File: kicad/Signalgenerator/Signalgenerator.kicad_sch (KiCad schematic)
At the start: 18 parts, among them U1 LT1354CS8, U2 LT1354CS8, U3 LT1354CS8, U4 LT1354CS8, U5 LT1354CS8, U6 LT1354CS8, U7 LT1354CS8

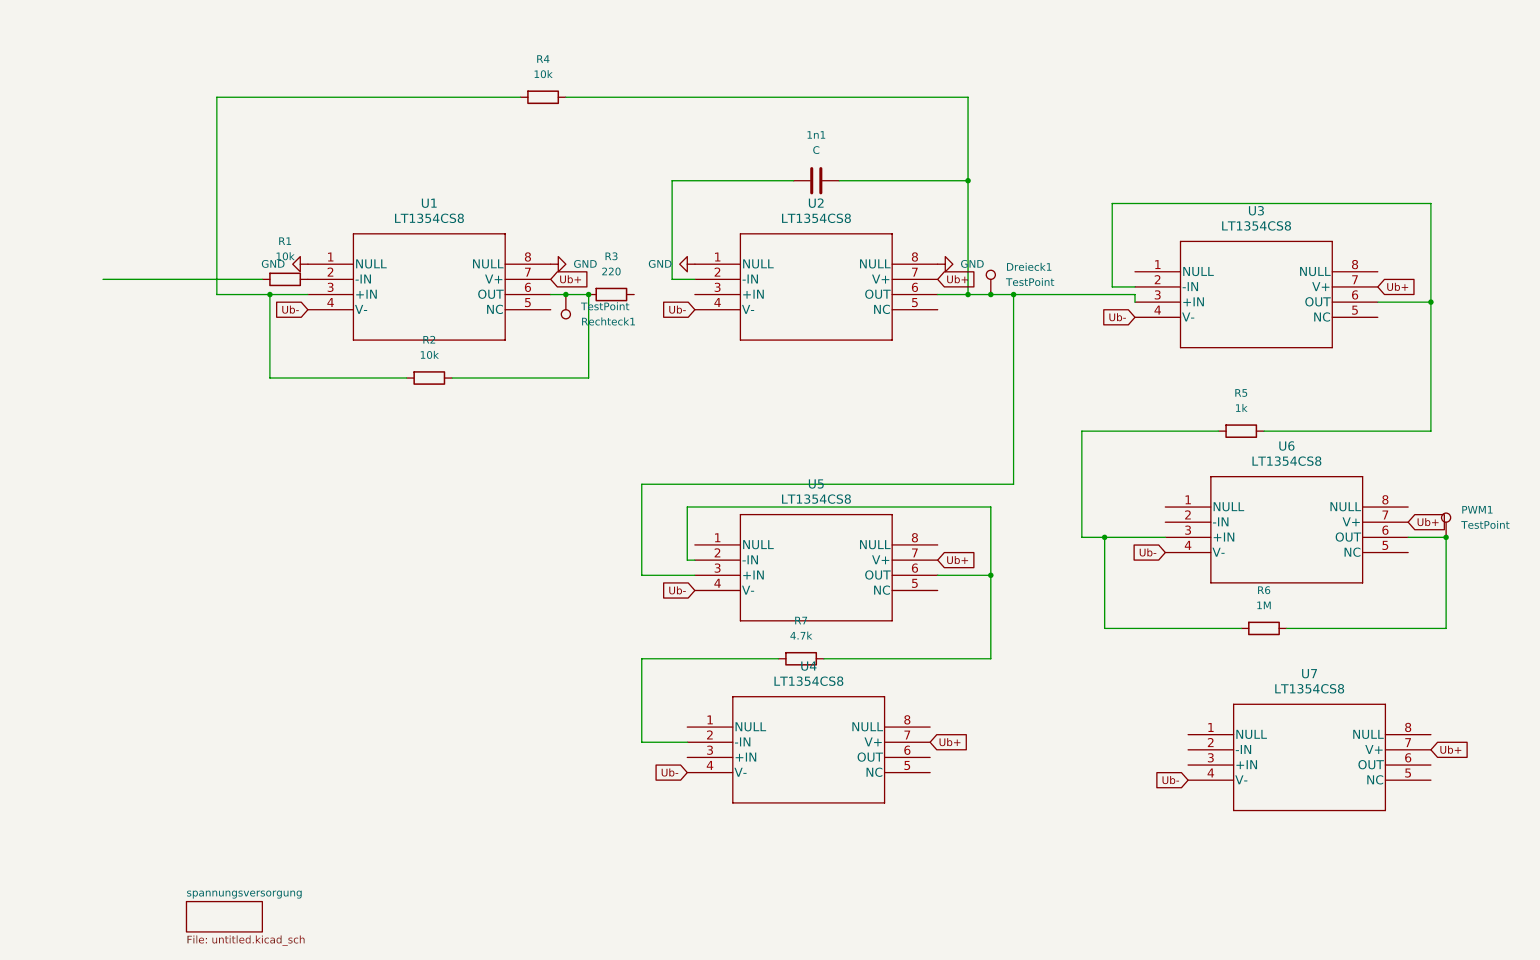
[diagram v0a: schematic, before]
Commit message: Platine layout angefangen. Probleme mit Überkreuzungen.
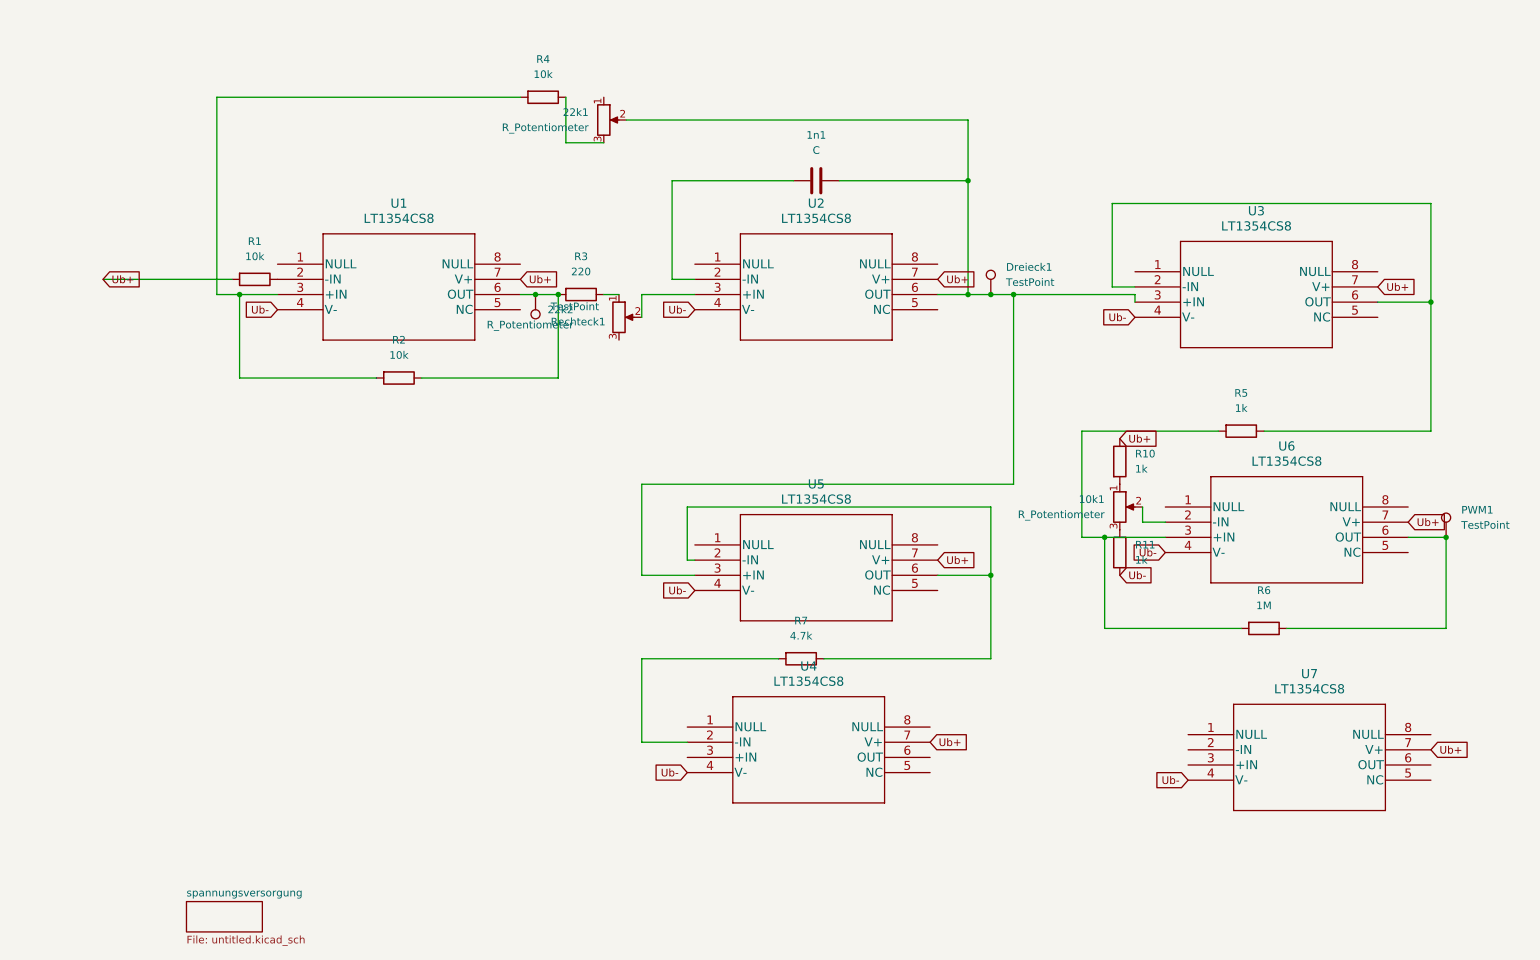
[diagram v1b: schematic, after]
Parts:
- added 10k1, 22k1, 22k2: R_Potentiometer, Potentiometer_THT:Potentiometer_Vishay_T7-YA_Single_Vertical, symbol Device:R_Potentiometer
- added R10, R11: 1k, Resistor_SMD:R_0805_2012Metric_Pad1.20x1.40mm_HandSolder, symbol Device:R
- 1n1: footprint (none) -> Capacitor_SMD:C_0603_1608Metric_Pad1.08x0.95mm_HandSolder
- R1, R2, R3, R4, R5, R6, R7: footprint (none) -> Resistor_SMD:R_0805_2012Metric_Pad1.20x1.40mm_HandSolder
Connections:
- net Ub+: now also R1.2, R10.1
- net Ub-: now also R11.1
- net at 1n1.1, Dreieck1.1, U2.6 (OUT)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: now also 22k1.2; no longer R4.1
- net at R3.1: now also 22k2.1
- net at U2.3 (+IN): now also 22k2.2
- net at U6.2 (-IN): now also 10k1.2
- removed net GND: U1.1 (NULL), U1.8 (NULL), U2.1 (NULL), U2.8 (NULL)
- new net: 22k1.3, R4.1
- new net: 10k1.3, R11.2
- new net: 10k1.1, R10.2
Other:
- moved on the sheet: R1, R2, R3, Rechteck1, U1

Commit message: kleine änderungen
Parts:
- R4: value 10k -> 1k
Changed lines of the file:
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@@
 			)
 		)
-		(property "Value" "10k"
+		(property "Value" "1k"
 			(at 106.68 21.59 90)
 			(effects

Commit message: layout zwischenstand
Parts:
- added C10, C11, C12, C13, C14, C15, C16, C17, C18, C19, C20, C7, C8, C9: 0.1u, Capacitor_SMD:C_0603_1608Metric_Pad1.08x0.95mm_HandSolder, symbol Device:C
- added C22: 1n, Capacitor_SMD:C_0603_1608Metric_Pad1.08x0.95mm_HandSolder, symbol Device:C
- added C23: 100p, Capacitor_SMD:C_0603_1608Metric_Pad1.08x0.95mm_HandSolder, symbol Device:C
- added C6: 10n, Capacitor_SMD:C_0603_1608Metric_Pad1.08x0.95mm_HandSolder, symbol Device:C
- added D1: D, Diode_THT:D_A-405_P2.54mm_Vertical_AnodeUp, symbol Device:D
- added R12: 1k, Resistor_SMD:R_0805_2012Metric_Pad1.20x1.40mm_HandSolder, symbol Device:R
- added R13: 10k, Resistor_SMD:R_0805_2012Metric_Pad1.20x1.40mm_HandSolder, symbol Device:R
- added R14, R15, R16: 0, Resistor_SMD:R_0805_2012Metric_Pad1.20x1.40mm_HandSolder, symbol Device:R
- added RV1, RV2: R_Potentiometer, Potentiometer_THT:Potentiometer_Vishay_T7-YA_Single_Vertical, symbol Device:R_Potentiometer
- added SW1, SW3: OS103011MS8QP1, footprints:OS103011MS8QP1, symbol 2026-05-24_19-47-42:OS103011MS8QP1
- added SW2: SW_DPDT_x2, Button_Switch_THT:SW_Slide_SPDT_Straight_CK_OS102011MS2Q, symbol Switch:SW_DPDT_x2
- C24: renamed from 1n1; value C -> 10n
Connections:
- net Ub+: now also C10.2, C12.2, C14.2, C16.2, C18.2, C20.2, C8.2, R14.1, R14.2, RV2.1
- net Ub-: now also C11.1, C13.1, C15.1, C17.1, C19.1, C7.1, C9.1, R15.1, R15.2, RV2.3
- net at Dreieck1.1, U2.6 (OUT), U5.3 (+IN): now also R16.2, SW1.2, SW3.3; no longer 22k1.2, C24.1, U3.3 (+IN)
- net at C24.2, U2.2 (-IN): now also 22k1.2, C22.1, C23.1
- net at 22k2.1, R3.1: now also D1.2 (A)
- net at 22k2.2: now also SW2.1 (A); no longer U2.3 (+IN)
- net at R5.2, R6.2, U6.3 (+IN): now also SW3.1
- net at U7.2 (-IN): now also R12.2, RV1.3
- net at U7.3 (+IN): now also SW3.2
- net at U7.6 (OUT): now also RV1.2
- net at R7.2, U4.2 (-IN): now also C6.2, R13.2
- net GND: now reaches U4.3 (+IN)
- net GND: now also C10.1, C11.2, C12.1, C13.2, C14.1, C15.2, C16.1, C17.2, C18.1, C19.2, C20.1, C7.2, C8.1, C9.2
- net at U4.6 (OUT): now also C6.1, R13.1, SW3.4
- new net: R12.1, RV2.2
- new net: R16.1, U3.3 (+IN)
- new net: C24.1, SW1.1
- new net: C23.2, SW1.4
- new net: D1.1 (K), SW2.3 (C)
- new net: C22.2, SW1.3
- new net: SW2.2 (B), U2.3 (+IN)
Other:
- moved on the sheet: 22k1, 22k2, R1, R2, R3, R4, R7, Rechteck1, U1, U4, U5

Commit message: aktueller stand
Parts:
- added R17, R18: 0, Resistor_SMD:R_0805_2012Metric_Pad1.20x1.40mm_HandSolder, symbol Device:R
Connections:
- net at Dreieck1.1, R16.2, SW1.2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: now also R17.1; no longer U2.6 (OUT)
- net at 22k1.2, C22.1, C23.1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: now also R18.1; no longer U2.2 (-IN)
- new net: R17.2, U2.6 (OUT)
- new net: R18.2, U2.2 (-IN)
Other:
- moved on the sheet: D1, Dreieck1, SW2A

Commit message: schaltplan angepasst
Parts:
- removed C11, C13, C15, C17, C19, C7, C9: 0.1u, Capacitor_SMD:C_0603_1608Metric_Pad1.08x0.95mm_HandSolder, symbol Device:C
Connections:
- net GND: no longer C10.1, C12.1, C14.1, C16.1, C18.1, C20.1, C8.1
- net Ub-: now also C10.1, C12.1, C14.1, C16.1, C18.1, C20.1, C8.1

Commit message: stand jetzt
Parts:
- removed R16, R17, R18: 0, Resistor_SMD:R_0805_2012Metric_Pad1.20x1.40mm_HandSolder, symbol Device:R
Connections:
- net at U3.3 (+IN): now also Dreieck1.1, SW1.2, SW3.3, U2.6 (OUT), U5.3 (+IN)
- net at 22k1.2, C22.1, C23.1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: now also U2.2 (-IN)
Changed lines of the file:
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@@
 	)
 	(junction
-		(at 185.42 58.42)
+		(at 90.17 58.42)
 		(diameter 0)
 		(color 0 0 0 0)
 	)
 	(junction
-		(at 90.17 58.42)
+		(at 181.61 58.42)
 		(diameter 0)
 		(color 0 0 0 0)
 	)
 	(junction
-		(at 181.61 58.42)
+		(at 185.42 58.42)
 		(diameter 0)
 		(color 0 0 0 0)
@@
 	(wire
 		(pts
-			(xy 172.72 58.42) (xy 173.99 58.42)
+			(xy 172.72 58.42) (xy 181.61 58.42)
 		)
 		(stroke
@@
 	(wire
 		(pts
-			(xy 128.27 55.88) (xy 128.27 49.53)
-		)
-		(stroke
-			(width 0)
-			(type default)
-		)
-	)
-	(wire
-		(pts
 			(xy 92.71 101.6) (xy 91.44 101.6)
 		)
@@
 	(wire
 		(pts
-			(xy 128.27 41.91) (xy 128.27 39.37)
+			(xy 128.27 39.37) (xy 128.27 55.88)
 		)
 		(stroke
@@
 	(wire
 		(pts
-			(xy 193.04 58.42) (xy 205.74 58.42)
+			(xy 83.82 87.63) (xy 83.82 104.14)
 		)
 		(stroke
@@
 	(wire
 		(pts
-			(xy 83.82 87.63) (xy 83.82 104.14)
+			(xy 132.08 22.86) (xy 125.73 22.86)
 		)
 		(stroke
@@
 	(wire
 		(pts
-			(xy 132.08 22.86) (xy 125.73 22.86)
+			(xy 179.07 22.86) (xy 179.07 49.53)
 		)
 		(stroke
@@
 	(wire
 		(pts
-			(xy 179.07 22.86) (xy 179.07 49.53)
+			(xy 91.44 101.6) (xy 91.44 92.71)
 		)
 		(stroke
@@
 	(wire
 		(pts
-			(xy 91.44 101.6) (xy 91.44 92.71)
+			(xy 101.6 58.42) (xy 104.14 58.42)
 		)
 		(stroke
@@
 	(wire
 		(pts
-			(xy 101.6 58.42) (xy 104.14 58.42)
+			(xy 125.73 58.42) (xy 132.08 58.42)
 		)
 		(stroke
@@
 	(wire
 		(pts
-			(xy 125.73 58.42) (xy 132.08 58.42)
+			(xy 210.82 96.52) (xy 207.01 96.52)
 		)
 		(stroke
@@
 	(wire
 		(pts
-			(xy 210.82 96.52) (xy 207.01 96.52)
+			(xy 185.42 58.42) (xy 205.74 58.42)
 		)
 		(stroke
@@
 	)
 	(symbol
-		(lib_name "R_8")
-		(lib_id "Device:R")
-		(at 189.23 58.42 270)
-		(unit 1)
-		(exclude_from_sim no)
-		(in_bom yes)
-		(on_board yes)
-		(dnp no)
-		(fields_autoplaced yes)
-		(property "Reference" "R16"
-			(at 189.23 52.07 90)
-			(effects
-				(font
-					(size 1.27 1.27)
-				)
-			)
-		)
-		(property "Value" "0"
-			(at 189.23 54.61 90)
-			(effects
-				(font
-					(size 1.27 1.27)
-				)
-			)
-		)
-		(property "Footprint" "Resistor_SMD:R_0805_2012Metric_Pad1.20x1.40mm_HandSolder"
-			(at 189.23 56.642 90)
-			(effects
-				(font
-					(size 1.27 1.27)
-				)
-				(hide yes)
-			)
-		)
-		(property "Datasheet" "~"
-			(at 189.23 58.42 0)
-			(effects
-				(font
-					(size 1.27 1.27)
-				)
-				(hide yes)
-			)
-		)
-		(property "Description" "Resistor"
-			(at 189.23 58.42 0)
-			(effects
-				(font
-					(size 1.27 1.27)
-				)
-				(hide yes)
-			)
-		)
-		(pin "2"
-		)
-		(pin "1"
-		)
-		(instances
-			(project "Signalgenerator"
-				(path "/8862b47a-3c46-4bfb-a99b-c8e005d2d344"
-					(reference "R16")
-					(unit 1)
-				)
-			)
-		)
-	)
-	(symbol
 		(lib_name "R_Potentiometer_1")
 		(lib_id "Device:R_Potentiometer")
@@
 	)
 	(symbol
-		(lib_name "R_9")
-		(lib_id "Device:R")
-		(at 177.8 58.42 270)
-		(unit 1)
-		(exclude_from_sim no)
-		(in_bom yes)
-		(on_board yes)
-		(dnp no)
-		(fields_autoplaced yes)
-		(property "Reference" "R17"
-			(at 177.8 52.07 90)
-			(effects
-				(font
-					(size 1.27 1.27)
-				)
-			)
-		)
-		(property "Value" "0"
-			(at 177.8 54.61 90)
-			(effects
-				(font
-					(size 1.27 1.27)
-				)
-			)
-		)
-		(property "Footprint" "Resistor_SMD:R_0805_2012Metric_Pad1.20x1.40mm_HandSolder"
-			(at 177.8 56.642 90)
-			(effects
-				(font
-					(size 1.27 1.27)
-				)
-				(hide yes)
-			)
-		)
-		(property "Datasheet" "~"
-			(at 177.8 58.42 0)
-			(effects
-				(font
-					(size 1.27 1.27)
-				)
-				(hide yes)
-			)
-		)
-		(property "Description" "Resistor"
-			(at 177.8 58.42 0)
-			(effects
-				(font
-					(size 1.27 1.27)
-				)
-				(hide yes)
-			)
-		)
-		(pin "2"
-		)
-		(pin "1"
-		)
-		(instances
-			(project "Signalgenerator"
-				(path "/8862b47a-3c46-4bfb-a99b-c8e005d2d344"
-					(reference "R17")
-					(unit 1)
-				)
-			)
-		)
-	)
-	(symbol
 		(lib_name "C_1")
 		(lib_id "Device:C")
@@
 					(unit 1)
 				)
-			)
-		)
-	)
-	(symbol
-		(lib_name "R_10")
-		(lib_id "Device:R")
-		(at 128.27 45.72 0)
-		(unit 1)
-		(exclude_from_sim no)
-		(in_bom yes)
-		(on_board yes)
-		(dnp no)
-		(fields_autoplaced yes)
-		(property "Reference" "R18"
-			(at 130.81 44.4499 0)
-			(effects
-				(font
-					(size 1.27 1.27)
-				)
-				(justify left)
-			)
-		)
-		(property "Value" "0"
-			(at 130.81 46.9899 0)
-			(effects
-				(font
-					(size 1.27 1.27)
-				)
-				(justify left)
-			)
-		)
-		(property "Footprint" "Resistor_SMD:R_0805_2012Metric_Pad1.20x1.40mm_HandSolder"
-			(at 126.492 45.72 90)
-			(effects
-				(font
-					(size 1.27 1.27)
-				)
-				(hide yes)
-			)
-		)
-		(property "Datasheet" "~"
-			(at 128.27 45.72 0)
-			(effects
-				(font
-					(size 1.27 1.27)
-				)
-				(hide yes)
-			)
-		)
-		(property "Description" "Resistor"
-			(at 128.27 45.72 0)
-			(effects
-				(font
-					(size 1.27 1.27)
-				)
-				(hide yes)
-			)
-		)
-		(pin "2"
-		)
-		(pin "1"
-		)
-		(instances
-			(project "Signalgenerator"
-				(path "/8862b47a-3c46-4bfb-a99b-c8e005d2d344"
-					(reference "R18")
-					(unit 1)
-				)
